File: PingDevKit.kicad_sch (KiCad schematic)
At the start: 54 parts, among them J101 POWER, J102 DEBUG, J103 PORT1, J104 FPGA, J105 ETHERNET, J106 SYNC, J107 SONAR+, J108 SONAR+, J109 SONAR-, J110 SONAR-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

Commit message: various improvements
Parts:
- J103: value PORT1 -> ETHERNET
- T101: value B65655B0010X000 -> TRANSFORMER
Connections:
- net VCC renamed VTX
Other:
- sheet MCU ports: added VTX_EN, VTX_MODE; removed VCC_EN, VCC_MODE
- sheet Power ports: added VTX, VTX_EN, VTX_MODE; removed VCC, VCC_EN, VCC_MODE
- sheet TX ports: added VTX; removed VCC
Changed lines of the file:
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@@
 		)
 	)
-	(label "VCC_MODE"
+	(label "VTX_MODE"
 		(at 163.83 64.77 0)
 		(effects
@@
 		)
 	)
-	(label "VCC_MODE"
+	(label "VTX_MODE"
 		(at 361.95 165.1 180)
 		(effects
@@
 		)
 	)
-	(label "VCC_EN"
+	(label "VTX_EN"
 		(at 361.95 161.29 180)
 		(effects
@@
 		)
 	)
-	(label "VCC_EN"
+	(label "VTX_EN"
 		(at 163.83 60.96 0)
 		(effects
@@
 			)
 		)
-		(property "Value" "VCC"
+		(property "Value" "VTX"
 			(at 251.46 45.974 0)
 			(effects
@@
 			)
 		)
-		(property "Value" "VCC"
+		(property "Value" "VTX"
 			(at 140.97 282.194 0)
 			(effects
@@
 			)
 		)
-		(property "Value" "VCC"
+		(property "Value" "VTX"
 			(at 140.97 316.484 0)
 			(effects
@@
 			)
 		)
-		(property "Value" "VCC"
+		(property "Value" "VTX"
 			(at 177.8 193.294 0)
 			(effects
@@
 			)
 		)
-		(property "Value" "PORT1"
+		(property "Value" "ETHERNET"
 			(at 64.77 229.87 0)
 			(effects
@@
 			)
 		)
-		(property "Value" "B65655B0010X000"
+		(property "Value" "TRANSFORMER"
 			(at 204.47 355.6 0)
 			(effects
@@
 			)
 		)
-		(pin "VCC" output
-			(at 227.33 62.23 0)
+		(pin "RX_5V" output
+			(at 227.33 58.42 0)
 			(effects
 				(font
@@
 			)
 		)
-		(pin "VCC_EN" input
-			(at 185.42 60.96 180)
+		(pin "VTX" output
+			(at 227.33 62.23 0)
 			(effects
 				(font
 					(size 1.27 1.27)
 				)
-				(justify left)
+				(justify right)
 			)
 		)
-		(pin "RX_5V" output
-			(at 227.33 58.42 0)
+		(pin "VTX_EN" input
+			(at 185.42 60.96 180)
 			(effects
 				(font
 					(size 1.27 1.27)
 				)
-				(justify right)
+				(justify left)
 			)
 		)
-		(pin "VCC_MODE" input
+		(pin "VTX_MODE" input
 			(at 185.42 64.77 180)
 			(effects
@@
 			)
 		)
-		(pin "VCC" input
-			(at 185.42 199.39 180)
-			(effects
-				(font
-					(size 1.27 1.27)
-				)
-				(justify left)
-			)
-		)
 		(pin "SONAR_TX_EN" input
 			(at 185.42 222.25 180)
@@
 			)
 		)
+		(pin "VTX" input
+			(at 185.42 199.39 180)
+			(effects
+				(font
+					(size 1.27 1.27)
+				)
+				(justify left)
+			)
+		)
 		(instances
 			(project "PingDevKit"
@@
 			)
 		)
-		(pin "VCC_EN" output
-			(at 340.36 161.29 0)
-			(effects
-				(font
-					(size 1.27 1.27)
-				)
-				(justify right)
-			)
-		)
-		(pin "VCC_MODE" output
-			(at 340.36 165.1 0)
-			(effects
-				(font
-					(size 1.27 1.27)
-				)
-				(justify right)
-			)
-		)
 		(pin "AUX_ANALOG" input
 			(at 290.83 231.14 180)
@@
 			)
 		)
+		(pin "VTX_EN" output
+			(at 340.36 161.29 0)
+			(effects
+				(font
+					(size 1.27 1.27)
+				)
+				(justify right)
+			)
+		)
+		(pin "VTX_MODE" output
+			(at 340.36 165.1 0)
+			(effects
+				(font
+					(size 1.27 1.27)
+				)
+				(justify right)
+			)
+		)

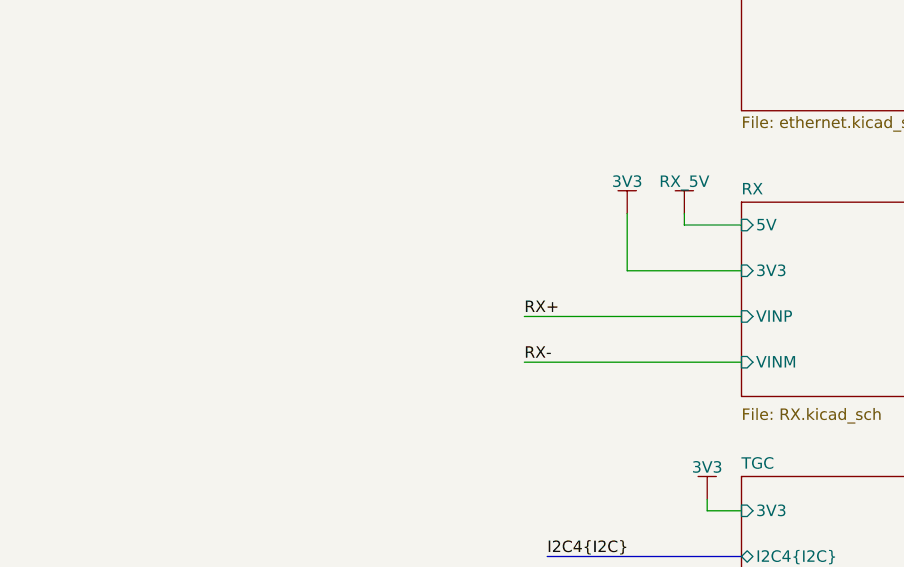
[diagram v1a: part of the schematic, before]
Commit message: added RC filters on RX power + new TIM8 pins
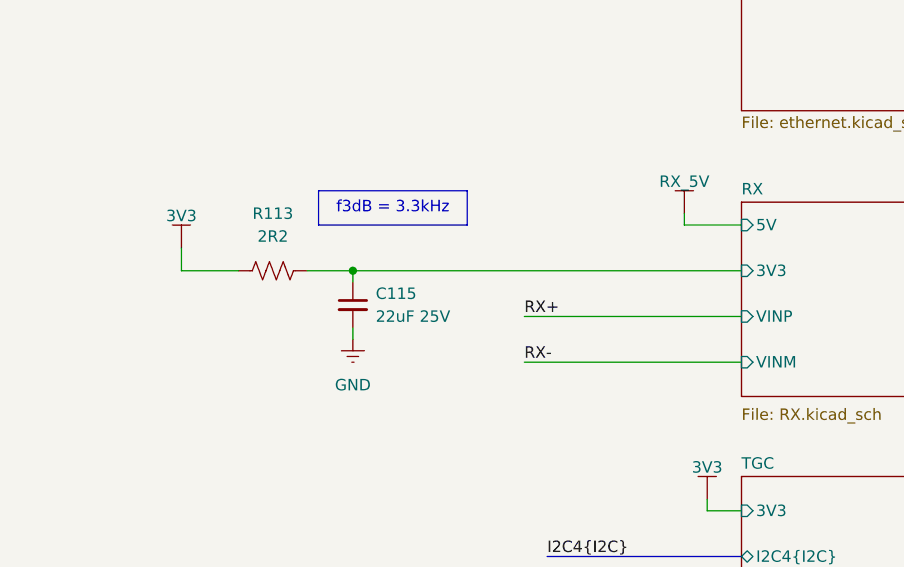
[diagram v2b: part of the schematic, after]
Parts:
- added C115: 22uF 25V, BR_Passives:C_0805_2012Metric-minimized, symbol BR_Capacitors_0805:C_0805_22uF_25V_X5R_20%
- added R113: 2R2, BR_Passives:R_0402_1005Metric-minimized, symbol BR_Resistors_0402:R_0402_2R2
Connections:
- net 3V3: now also R113.1
- net GND: now also C115.2
- new net RX/3V3: C115.1, R113.2

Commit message: last checks + board characteristics tables
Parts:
- C104, C113: JLCPCB Part Num (none) -> C76939
- C105: JLCPCB Part Num (none) -> C576517
- D101: JLCPCB Part Num (none) -> C894520
- J103: JLCPCB Part Num (none) -> C708645
- Q101: JLCPCB Part Num (none) -> C154911
- R101, R102: JLCPCB Part Num (none) -> C106235
- R103: JLCPCB Part Num (none) -> C138139
- R104, R111, R112: JLCPCB Part Num (none) -> C106225
- TH101: JLCPCB Part Num (none) -> C98098
- U101: JLCPCB Part Num (none) -> C110926
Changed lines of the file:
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@@
 		)
 	)
+	(text_box "CHANGELOG\nRev A:\n-Initial revision\n\n"
+		(exclude_from_sim no)
+		(at 463.55 36.83 0)
+		(size 68.58 44.45)
+		(margins 0.9525 0.9525 0.9525 0.9525)
+		(stroke
+			(width 0)
+			(type solid)
+		)
+		(fill
+			(type none)
+		)
+		(effects
+			(font
+				(size 1.27 1.27)
+			)
+			(justify left top)
+		)
+	)
 	(text_box "f3dB = 3.3kHz"
 		(exclude_from_sim no)
@@
 	(wire
 		(pts
-			(xy 68.58 264.16) (xy 71.12 264.16)
+			(xy 58.42 264.16) (xy 71.12 264.16)
 		)
 		(stroke
@@
 	(wire
 		(pts
-			(xy 68.58 261.62) (xy 68.58 264.16)
+			(xy 58.42 261.62) (xy 58.42 264.16)
 		)
 		(stroke
@@
 			)
 		)
+		(property "JLCPCB Part Num" "C894520"
+			(at 33.02 72.39 0)
+			(effects
+				(font
+					(size 1.27 1.27)
+				)
+				(justify left)
+				(hide yes)
+			)
+		)
 		(pin "1"
 		)
@@
 			)
 		)
+		(property "JLCPCB Part Num" "C154911"
+			(at 22.86 68.58 0)
+			(effects
+				(font
+					(size 1.27 1.27)
+				)
+				(justify left)
+				(hide yes)
+			)
+		)
 		(pin "1"
 		)
@@
 			)
 		)
+		(property "JLCPCB Part Num" "C138139"
+			(at 68.58 39.37 0)
+			(effects
+				(font
+					(size 1.27 1.27)
+				)
+				(justify left)
+				(hide yes)
+			)
+		)
 		(pin "2"
 		)
@@
 			)
 		)
+		(property "JLCPCB Part Num" "C106235"
+			(at 92.71 252.73 0)
+			(effects
+				(font
+					(size 1.27 1.27)
+				)
+				(justify left)
+				(hide yes)
+			)
+		)
 		(pin "1"
 		)
@@
 			)
 		)
+		(property "JLCPCB Part Num" "C110926"
+			(at 331.47 281.94 0)
+			(effects
+				(font
+					(size 1.27 1.27)
+				)
+				(justify left)
+				(hide yes)
+			)
+		)
 		(pin "3"
 		)
@@
 			)
 		)
+		(property "JLCPCB Part Num" "C576517"
+			(at 54.61 34.29 0)
+			(effects
+				(font
+					(size 1.27 1.27)
+				)
+				(justify left)
+				(hide yes)
+			)
+		)
 		(pin "1"
 		)
@@
 			)
 		)
+		(property "JLCPCB Part Num" "C98098"
+			(at 71.12 308.61 0)
+			(effects
+				(font
+					(size 1.27 1.27)
+				)
+				(justify left)
+				(hide yes)
+			)
+		)
 		(pin "2"
 		)
@@
 			)
 		)
+		(property "JLCPCB Part Num" "C106225"
+			(at 293.37 275.59 0)
+			(effects
+				(font
+					(size 1.27 1.27)
+				)
+				(justify left)
+				(hide yes)
+			)
+		)
 		(pin "2"
 		)
@@
 			)
 		)
-		(property "Description" "100nF 25V X7R 10% Ceramic Capacitor 0201"
+		(property "Description" "100nF 25V X5R 10% Ceramic Capacitor 0201"
 			(at 321.31 243.84 0)
 			(effects
@@
 			)
 		)
+		(property "JLCPCB Part Num" "C76939"
+			(at 321.31 261.62 0)
+			(effects
+				(font
+					(size 1.27 1.27)
+				)
+				(justify left)
+				(hide yes)
+			)
+		)
 		(pin "1"
 		)
@@
 			)
 		)
+		(property "JLCPCB Part Num" "C106225"
+			(at 71.12 297.18 0)
+			(effects
+				(font
+					(size 1.27 1.27)
+				)
+				(justify left)
+				(hide yes)
+			)
+		)
 		(pin "2"
 		)
@@
 			)
 		)
-		(property "Description" "100nF 25V X7R 10% Ceramic Capacitor 0201"
+		(property "Description" "100nF 25V X5R 10% Ceramic Capacitor 0201"
 			(at 53.34 290.83 0)
 			(effects
@@
 			)
 		)
+		(property "JLCPCB Part Num" "C76939"
+			(at 53.34 308.61 0)
+			(effects
+				(font
+					(size 1.27 1.27)
+				)
+				(justify left)
+				(hide yes)
+			)
+		)
 		(pin "1"
 		)
@@
 			)
 		)
+		(property "JLCPCB Part Num" "C106235"
+			(at 92.71 237.49 0)
+			(effects
+				(font
+					(size 1.27 1.27)
+				)
+				(justify left)
+				(hide yes)
+			)
+		)
 		(pin "1"
 		)
@@
 			)
 		)
+		(property "JLCPCB Part Num" "C708645"
+			(at 55.88 189.23 0)
+			(effects
+				(font
+					(size 1.27 1.27)
+				)
+				(justify left)
+				(hide yes)
+			)
+		)
 		(pin "12"
 		)
@@
 				(hide yes)
 			)
+		)
+		(property "JLCPCB Part Num" "C106225"
+			(at 300.99 275.59 0)
+			(effects
+				(font
+					(size 1.27 1.27)
+				)
+				(justify left)
+				(hide yes)
+			)

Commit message: Rev A release files
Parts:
- C114: symbol BR_Capacitors_0402:C_0402_1uF_50V_X5R_20% -> BR_Capacitors_0402:C_0402_1uF_50V_X5R_10%; JLCPCB Part Num (none) -> C1518208
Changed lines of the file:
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@@
 			)
 		)
+		(property "Sim.Enable" "0"
+			(at 30.48 25.4 0)
+			(effects
+				(font
+					(size 1.27 1.27)
+				)
+				(hide yes)
+			)
+		)
 		(pin "1"
 		)
@@
 			)
 		)
+		(property "Sim.Enable" "0"
+			(at 83.82 25.4 0)
+			(effects
+				(font
+					(size 1.27 1.27)
+				)
+				(hide yes)
+			)
+		)
 		(pin "1"
 		)
@@
 	)
 	(symbol
-		(lib_id "BR_Capacitors_0402:C_0402_1uF_50V_X5R_20%")
+		(lib_id "BR_Capacitors_0402:C_0402_1uF_50V_X5R_10%")
 		(at 331.47 307.34 180)
 		(unit 1)
@@
 			)
 		)
-		(property "Description" "1uF 50V X5R 5% Ceramic Capacitor 0402"
+		(property "Description" "1uF 50V X5R 10% Ceramic Capacitor 0402"
 			(at 331.47 370.84 0)
 			(effects
@@
 			)
 		)
+		(property "JLCPCB Part Num" "C1518208"
+			(at 331.47 353.06 0)
+			(effects
+				(font
+					(size 1.27 1.27)
+				)
+				(justify left)
+				(hide yes)
+			)
+		)
 		(pin "2"
 		)
@@
 			)
 		)
+		(property "Sim.Enable" "0"
+			(at 48.26 25.4 0)
+			(effects
+				(font
+					(size 1.27 1.27)
+				)
+				(hide yes)
+			)
+		)
 		(pin "1"
 		)
@@
 			(effects
 				(font
+					(size 1.27 1.27)
+				)
+				(hide yes)
+			)
+		)
+		(property "Sim.Enable" "0"
+			(at 66.04 25.4 0)
+			(effects
+				(font

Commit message: fixing JLC rules
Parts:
- removed C115: 22uF 25V, BR_Passives:C_0805_2012Metric-minimized, symbol BR_Capacitors_0805:C_0805_22uF_25V_X5R_20%
- removed R113: 2R2, BR_Passives:R_0402_1005Metric-minimized, symbol BR_Resistors_0402:R_0402_2R2
- C104, C113: JLCPCB Part Num C76939 -> (none)
- C105: JLCPCB Part Num C576517 -> (none)
- C114: symbol BR_Capacitors_0402:C_0402_1uF_50V_X5R_10% -> BR_Capacitors_0402:C_0402_1uF_50V_X5R_20%; JLCPCB Part Num C1518208 -> (none)
- D101: JLCPCB Part Num C894520 -> (none)
- J103: JLCPCB Part Num C708645 -> (none)
- Q101: JLCPCB Part Num C154911 -> (none)
- R101, R102: JLCPCB Part Num C106235 -> (none)
- R103: JLCPCB Part Num C138139 -> (none)
- R104, R111, R112: JLCPCB Part Num C106225 -> (none)
- TH101: JLCPCB Part Num C98098 -> (none)
- U101: JLCPCB Part Num C110926 -> (none)
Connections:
- no-connect marks 10 -> 11

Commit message: refactoring tx a bit
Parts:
- removed R105, R106, R107, R108: 100k, BR_Passives:C_0402_1005Metric-minimized, symbol BR_Resistors_0402:R_0402_100k
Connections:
- net TX+: now also T101.2 (TX-); no longer T101.1 (TX+)
- net TX-: now also T101.1 (TX+); no longer T101.2 (TX-)

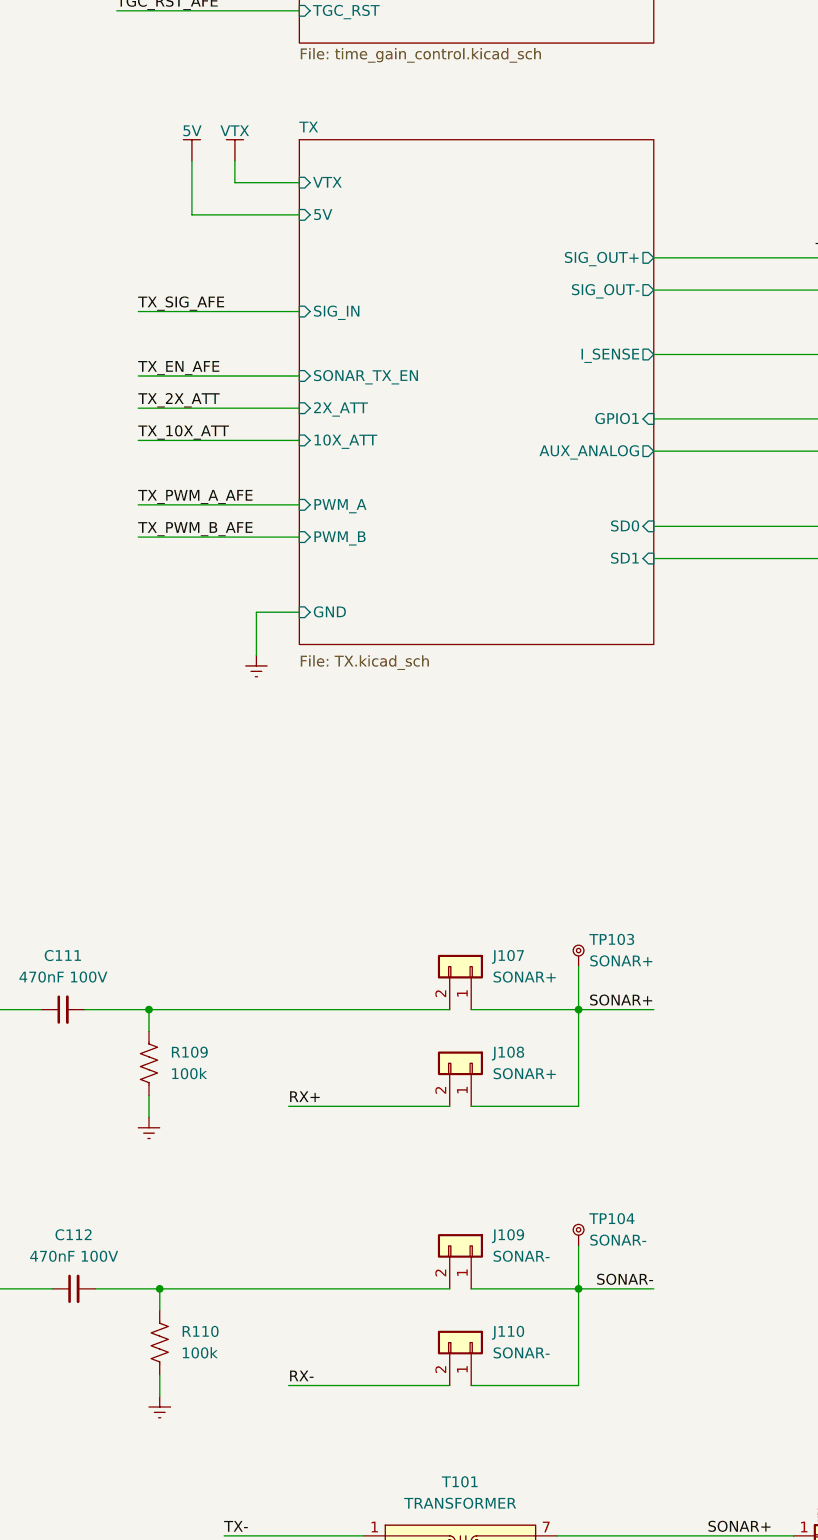
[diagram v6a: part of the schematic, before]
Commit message: Various changes to TX connectity
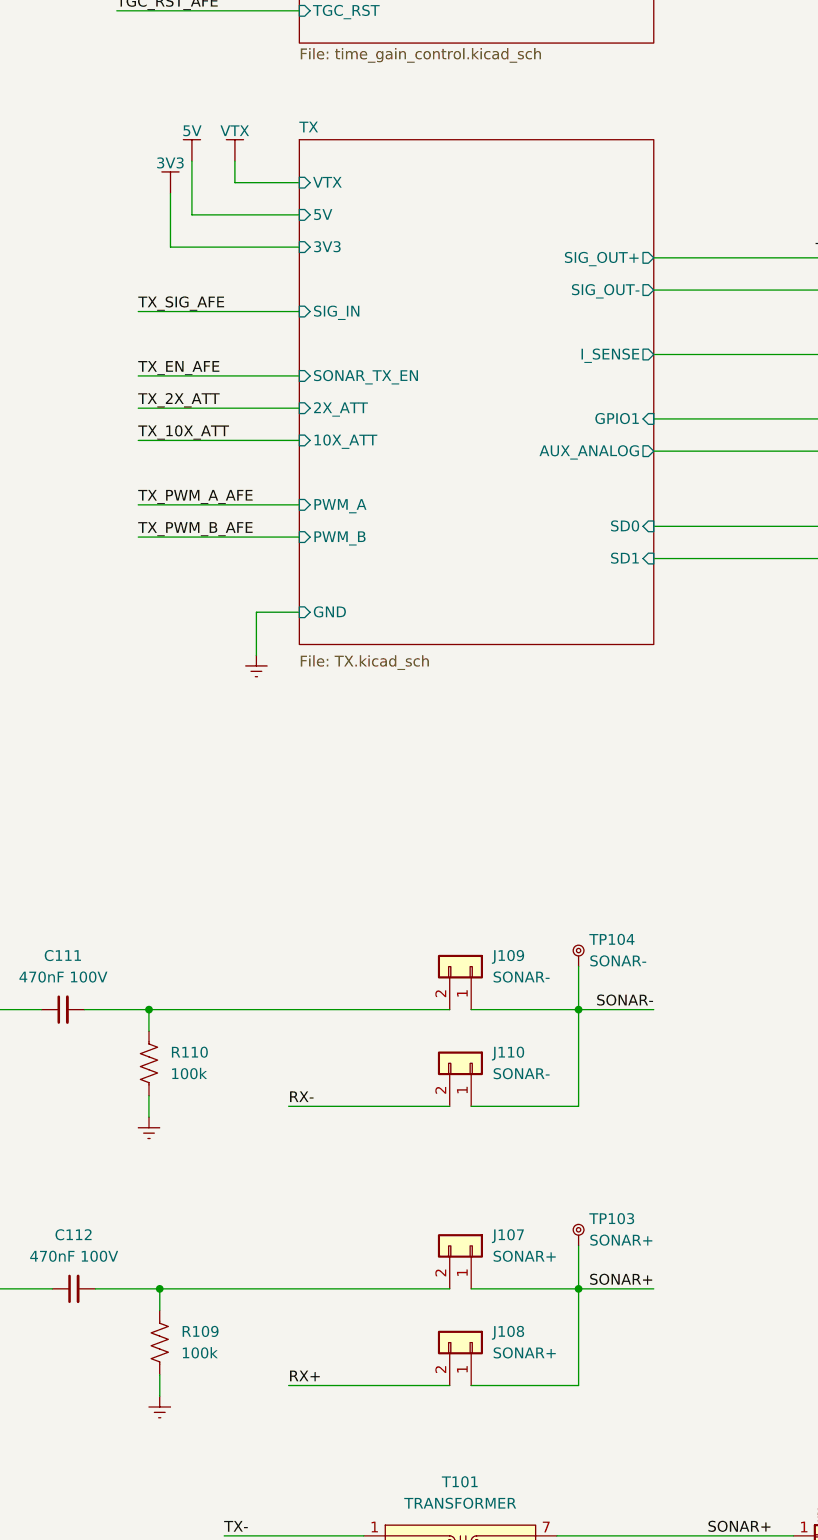
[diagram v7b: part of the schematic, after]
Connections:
- net at J107.2 (Pin_2), R109.1: now also C112.2; no longer C111.2
- net at J109.2 (Pin_2), R110.1: now also C111.2; no longer C112.2
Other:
- sheet TX ports: added 3V3; removed none
- moved on the sheet: J107, J108, J109, J110, R109, R110, TP103, TP104

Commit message: some tweaks
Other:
- note added: "Swapped TX polarity to simplify routing"
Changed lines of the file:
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@@
+		)
+	)
+	(text "Swapped TX polarity to simplify routing"
+		(exclude_from_sim no)
+		(at 154.178 355.854 0)
+		(effects
+			(font
+				(size 1.27 1.27)
+			)
 		)
 	)
